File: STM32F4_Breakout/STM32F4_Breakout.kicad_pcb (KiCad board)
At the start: 4 copper layers, 50 x 49.8 mm, 44 parts, among them J1 Conn_01x02, J2 Conn_01x02, J3 Conn_01x02, J4 Conn_02x05_Odd_Even, J5 Conn_01x04, J6 Conn_01x02, U1 AMS1117-3.3, U2 STM32F405RGT6

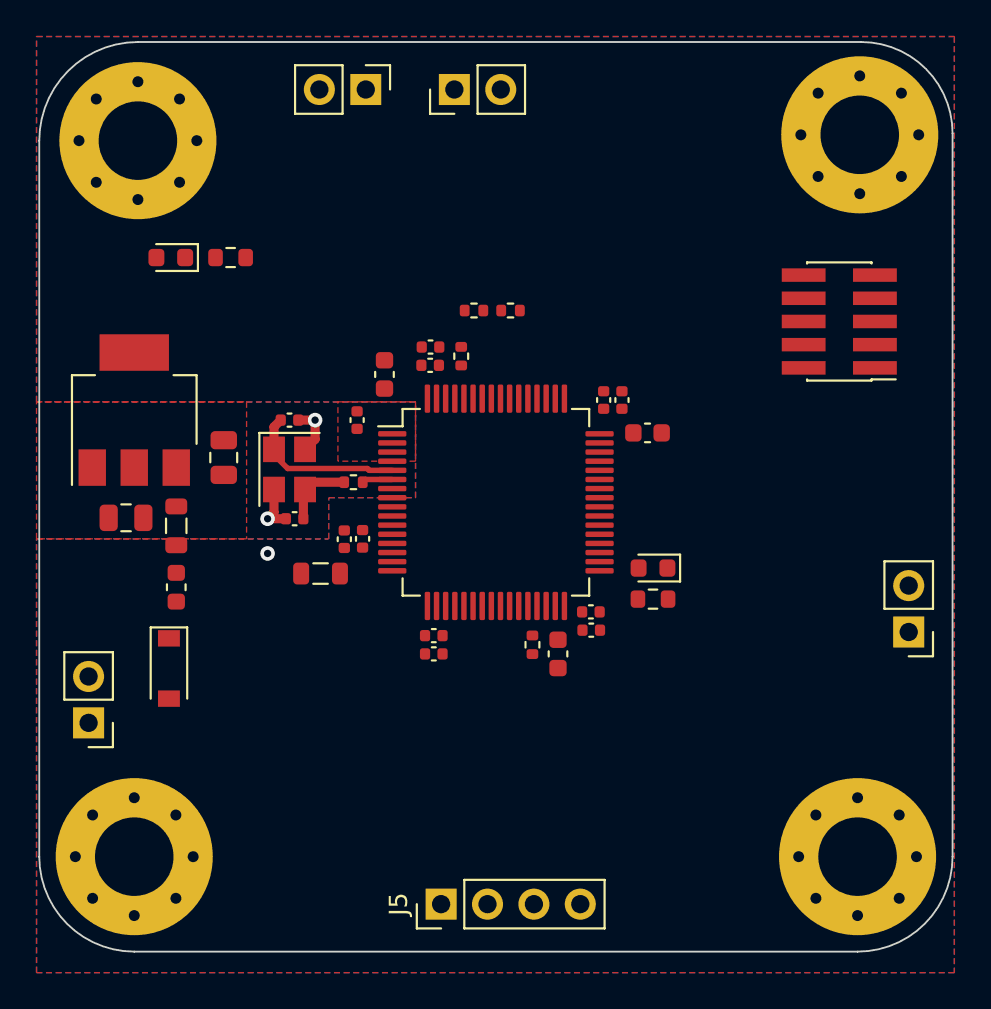
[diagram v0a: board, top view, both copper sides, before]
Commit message: routed power lines and debug connector
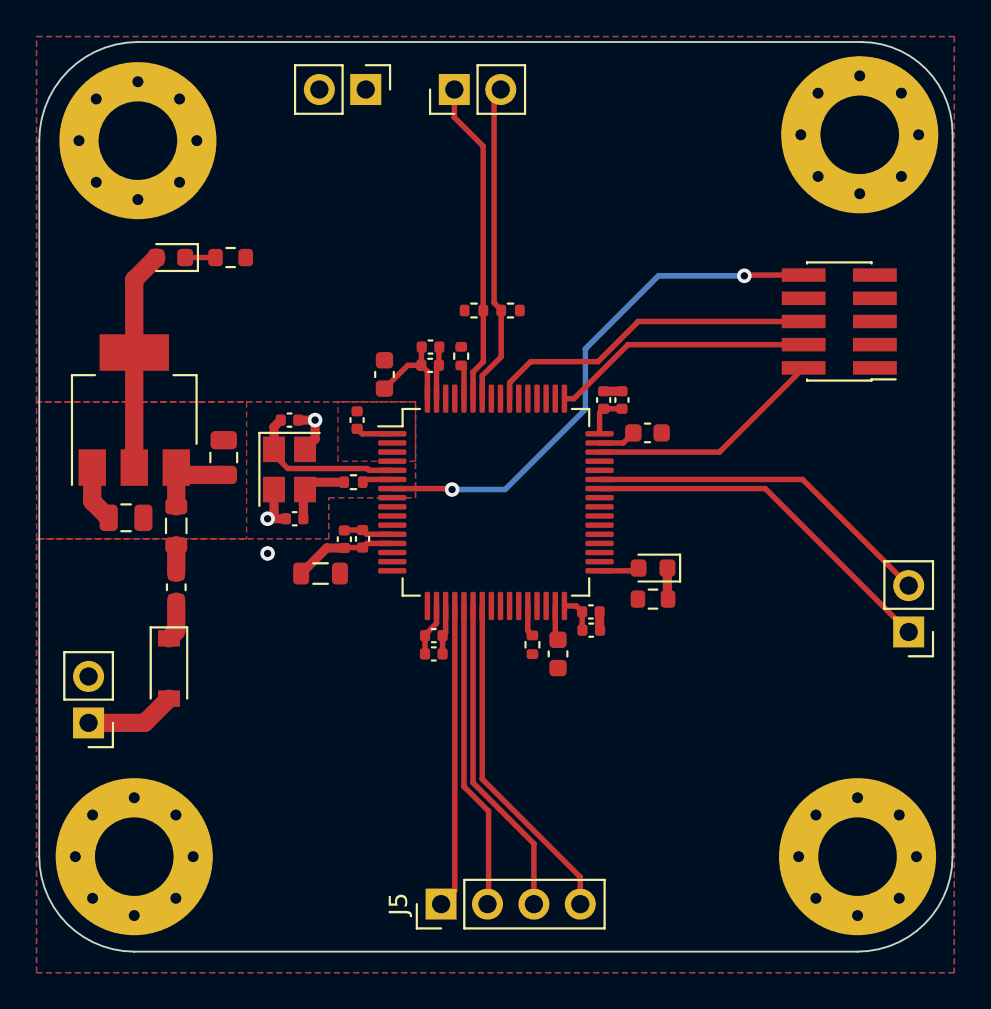
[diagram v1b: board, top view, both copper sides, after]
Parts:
- moved R2 2.00 mm to (86.2, 54.5), turned to 0 degrees
- moved R3 2.00 mm to (84.2, 54.5)
- turned C7 to 0 degrees
- turned C8 to 0 degrees
- turned FB1 to 90 degrees
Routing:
- net NRST: track 0.00 -> 29.3 mm, vias 0 -> 2
- net +3V3: track 0.00 -> 26.8 mm
- net USART1_TX: track 0.00 -> 20.2 mm
- net USART1_RX: track 0.00 -> 19.3 mm
- net SPI1_MOSI: track 0.00 -> 18.5 mm
- net SWO: track 0.00 -> 18.4 mm
- net I2C1_SDA: track 0.00 -> 17.8 mm
- net SPI1_MISO: track 0.00 -> 17.7 mm
- net I2C1_SCL: track 0.00 -> 17.7 mm
- net SPI1_SCK: track 0.00 -> 16.9 mm
- net SPI1_CS: track 0.00 -> 16.6 mm
- net SWCLK: track 0.00 -> 14.3 mm
- net GND: track 7.39 -> 21.0 mm
- net SWDIO: track 0.00 -> 13.1 mm
- net +3.3VA: track 0.00 -> 5.67 mm
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
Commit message: power and ground connections (vias)
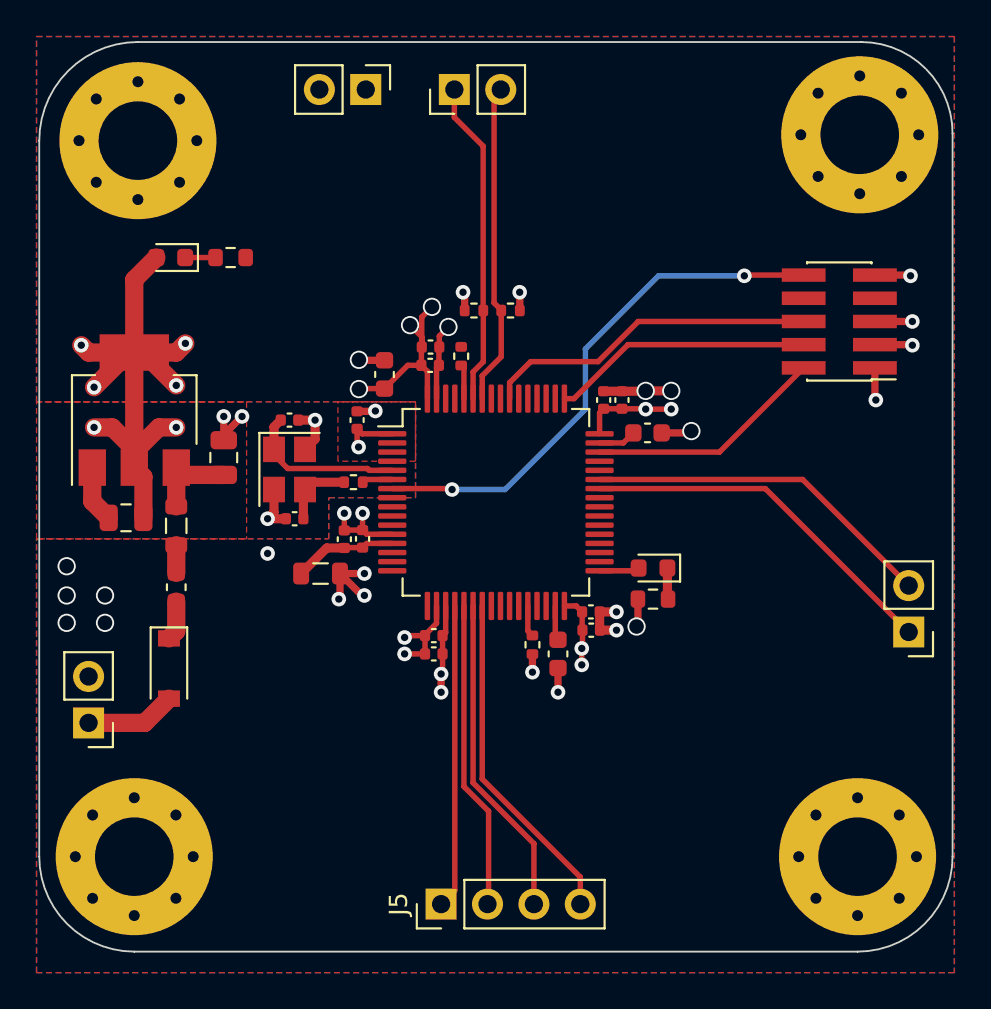
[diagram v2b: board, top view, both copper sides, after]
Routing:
- net +3V3: track 26.8 -> 70.8 mm, vias 0 -> 22
- net GND: track 21.0 -> 48.0 mm, vias 3 -> 28

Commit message: silkscreen labeling; gerber and drill file generation; BoM
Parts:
- moved D1 1.70 mm to (69.2, 74.1)
- moved D2 1.00 mm to (67.6, 52.6)
- moved R1 1.00 mm to (70.9, 52.6)
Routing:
- net VCC: track 4.95 -> 6.65 mm
- net +3V3: track 70.8 -> 69.8 mm
- net Net-(D1-Pad1): track 2.18 -> 3.08 mm
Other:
- board text added: "+"
- board text added: "3V3"
- board text added: "CS"
- board text added: "GND"
- board text added: "I2C"
- board text added: "MISO"
- board text added: "MOSI"
- board text added: "POWER"
- board text added: "RX"
- board text added: "SCK"
- board text added: "SCL"
- board text added: "SDA"
- board text added: "SPI"
- board text added: "STAT"
- board text added: "SWD"
- board text added: "TX"
- board text added: "UART"
- board text added: "VCC"
- board text added: "VIN"
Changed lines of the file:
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@@
       (outputformat 1)
       (mirror false)
-      (drillshape 1)
+      (drillshape 0)
       (scaleselection 1)
-      (outputdirectory "")
+      (outputdirectory "assembly/")
     )
   )
@@
   )
   (footprint "LED_SMD:LED_0603_1608Metric" (layer "F.Cu")
-    (at 67.6 51.6 180)
+    (at 67.6 52.6 180)
     (descr "LED SMD 0603 (1608 Metric), square (rectangular) end terminal, IPC_7351 nominal, (Body size source: http://www.tortai-tech.com/upload/download/2011102023233369053.pdf), generated with kicad-footprint-generator")
     (tags "LED")
@@
   )
   (footprint "Diode_SMD:D_SOD-123" (layer "F.Cu")
-    (at 67.5 74.1 -90)
+    (at 69.2 74.1 -90)
     (descr "SOD-123")
     (tags "SOD-123")
@@
   )
   (footprint "Resistor_SMD:R_0603_1608Metric" (layer "F.Cu")
-    (at 70.875 51.6 180)
+    (at 70.875 52.6 180)
     (descr "Resistor SMD 0603 (1608 Metric), square (rectangular) end terminal, IPC_7351 nominal, (Body size source: IPC-SM-782 page 72, https://www.pcb-3d.com/wordpress/wp-content/uploads/ipc-sm-782a_amendment_1_and_2.pdf), generated with kicad-footprint-generator")
     (tags "resistor")
@@
     )
   )
+  (gr_circle (center 108 57.75) (end 108 57.75) (layer "F.SilkS") (width 0.15) (fill none))
+  (gr_circle (center 78.55 61.225) (end 78.55 61.225) (layer "F.SilkS") (width 0.15) (fill none))
   (gr_line (start 110.4 44.8) (end 110.4 84.4) (layer "Edge.Cuts") (width 0.1))
   (gr_line (start 60.4 84.4) (end 60.4 45.2) (layer "Edge.Cuts") (width 0.1))
@@
   (gr_arc (start 110.4 84.4) (mid 108.876955 88.076955) (end 105.2 89.6) (layer "Edge.Cuts") (width 0.1))
   (gr_arc (start 60.4 45.2) (mid 61.981623 41.381623) (end 65.8 39.8) (layer "Edge.Cuts") (width 0.1))
+  (gr_text "TX" (at 104.6 72.1) (layer "B.SilkS")
+    (effects (font (size 1 1) (thickness 0.15)) (justify mirror))
+  )
+  (gr_text "GND" (at 75.8 45.8 90) (layer "B.SilkS")
+    (effects (font (size 1 1) (thickness 0.15)) (justify mirror))
+  )
+  (gr_text "RX" (at 104.7 69.5) (layer "B.SilkS")
+    (effects (font (size 1 1) (thickness 0.15)) (justify mirror))
+  )
+  (gr_text "MISO" (at 87.5 83.3 90) (layer "B.SilkS")
+    (effects (font (size 1 1) (thickness 0.15)) (justify mirror))
+  )
+  (gr_text "SDA" (at 83.1 45.8 90) (layer "B.SilkS")
+    (effects (font (size 1 1) (thickness 0.15)) (justify mirror))
+  )
+  (gr_text "SCK" (at 84.8 83.5 90) (layer "B.SilkS")
+    (effects (font (size 1 1) (thickness 0.15)) (justify mirror))
+  )
+  (gr_text "VCC" (at 66.5 77.4) (layer "B.SilkS")
+    (effects (font (size 1 1) (thickness 0.15)) (justify mirror))
+  )
+  (gr_text "CS" (at 82.3 83.4 90) (layer "B.SilkS")
+    (effects (font (size 1 1) (thickness 0.15)) (justify mirror))
+  )
+  (gr_text "MOSI" (at 90 83.3 90) (layer "B.SilkS")
+    (effects (font (size 1 1) (thickness 0.15)) (justify mirror))
+  )
+  (gr_text "GND" (at 66.6 74.5) (layer "B.SilkS")
+    (effects (font (size 1 1) (thickness 0.15)) (justify mirror))
+  )
+  (gr_text "SCL" (at 86.2 45.9 90) (layer "B.SilkS")
+    (effects (font (size 1 1) (thickness 0.15)) (justify mirror))
+  )
+  (gr_text "3V3" (at 78.6 45.8 90) (layer "B.SilkS")
+    (effects (font (size 1 1) (thickness 0.15)) (justify mirror))
+  )
+  (gr_text "+" (at 66.2 53.4) (layer "F.SilkS")
+    (effects (font (size 1 1) (thickness 0.15)))
+  )
+  (gr_text "UART" (at 105.1 70.8 90) (layer "F.SilkS")
+    (effects (font (size 1 1) (thickness 0.15)))
+  )
+  (gr_text "I2C" (at 84.7 45) (layer "F.SilkS")
+    (effects (font (size 1 1) (thickness 0.15)))
+  )
+  (gr_text "STAT" (at 93.9 67.1) (layer "F.SilkS")
+    (effects (font (size 1 1) (thickness 0.15)))
+  )
+  (gr_text "+" (at 92.5 69.2) (layer "F.SilkS")
+    (effects (font (size 1 1) (thickness 0.15)))
+  )
+  (gr_text "VIN" (at 65.8 75.3 90) (layer "F.SilkS")
+    (effects (font (size 1 1) (thickness 0.15)))
+  )
+  (gr_text "3V3" (at 67.4 51.1) (layer "F.SilkS")
+    (effects (font (size 1 1) (thickness 0.15)))
+  )
+  (gr_text "+" (at 70.4 76.4) (layer "F.SilkS")
+    (effects (font (size 1 1) (thickness 0.15)))
+  )
+  (gr_text "SPI" (at 86 84.4) (layer "F.SilkS")
+    (effects (font (size 1 1) (thickness 0.15)))
+  )
+  (gr_text "POWER" (at 77 45.1) (layer "F.SilkS")
+    (effects (font (size 1 1) (thickness 0.15)))
+  )
+  (gr_text "SWD" (at 104.2 60) (layer "F.SilkS")
+    (effects (font (size 1 1) (thickness 0.15)))
+  )
   (segment (start 70.5 61.3) (end 71.5 60.3) (width 0.4) (layer "F.Cu") (net 1))
   (segment (start 91.3 58.92) (end 92.3 58.92) (width 0.5) (layer "F.Cu") (net 1))
@@
   (segment (start 94.7875 70.2625) (end 94.825 70.3) (width 0.5) (layer "F.Cu") (net 2))
   (segment (start 94.7875 68.6) (end 94.7875 70.2625) (width 0.5) (layer "F.Cu") (net 2))
-  (segment (start 68.3875 51.6) (end 70.05 51.6) (width 0.3) (layer "F.Cu") (net 3))
+  (segment (start 68.3875 52.6) (end 70.05 52.6) (width 0.3) (layer "F.Cu") (net 3))
   (segment (start 83.65 57.66) (end 83.5 57.51) (width 0.3) (layer "F.Cu") (net 4))
   (segment (start 83.65 59.325) (end 83.65 57.66) (width 0.3) (layer "F.Cu") (net 4))
@@
   (segment (start 84.15 57.865894) (end 84.71 57.305894) (width 0.3) (layer "F.Cu") (net 8))
   (segment (start 93.58 59.88) (end 93.6 59.9) (width 0.3) (layer "F.Cu") (net 9))
-  (segment (start 65.6 52.8125) (end 66.8125 51.6) (width 1) (layer "F.Cu") (net 9))
+  (segment (start 65.6 53.8125) (end 66.8125 52.6) (width 1) (layer "F.Cu") (net 9))
   (segment (start 86.71 53.51) (end 86.7 53.5) (width 0.4) (layer "F.Cu") (net 9))
   (segment (start 66.1 56.8) (end 67.9 58.6) (width 1) (layer "F.Cu") (net 9))
@@
   (segment (start 65.6 63.1) (end 65.6 62.1) (width 1) (layer "F.Cu") (net 9))
   (segment (start 90.14 72) (end 90.14 72.96) (width 0.3) (layer "F.Cu") (net 9))
-  (segment (start 65.6 56.8) (end 65.6 52.8125) (width 1) (layer "F.Cu") (net 9))
   (segment (start 82.65 72.13) (end 82.48 72.3) (width 0.3) (layer "F.Cu") (net 9))
   (segment (start 65.6 62.1) (end 64.4 60.9) (width 1) (layer "F.Cu") (net 9))
@@
   (segment (start 80.575 57.5) (end 79.3 58.775) (width 0.3) (layer "F.Cu") (net 9))
   (segment (start 79.725 61.25) (end 78.07 61.25) (width 0.3) (layer "F.Cu") (net 9))
+  (segment (start 65.6 56.8) (end 65.6 53.8) (width 1) (layer "F.Cu") (net 9))
   (segment (start 90.14 72.96) (end 90.1 73) (width 0.3) (layer "F.Cu") (net 9))
   (segment (start 65.6 63.1) (end 65.6 56.8) (width 1) (layer "F.Cu") (net 9))
@@
   (segment (start 87.298959 57.3) (end 90.992894 57.3) (width 0.3) (layer "F.Cu") (net 58))
   (segment (start 67.9 67.35) (end 67.9 68.8625) (width 1) (layer "F.Cu") (net 63))
-  (segment (start 67.9 72.05) (end 67.5 72.45) (width 1) (layer "F.Cu") (net 64))
+  (segment (start 67.9 72.05) (end 68.8 72.05) (width 1) (layer "F.Cu") (net 64))
   (segment (start 67.9 70.4375) (end 67.9 72.05) (width 1) (layer "F.Cu") (net 64))
-  (segment (start 66.175 77.075) (end 67.5 75.75) (width 1) (layer "F.Cu") (net 65))
-  (segment (start 63.1 77.075) (end 66.175 77.075) (width 1) (layer "F.Cu") (net 65))
+  (segment (start 68.8 72.05) (end 69.2 72.45) (width 1) (layer "F.Cu") (net 64))
+  (segment (start 67.875 77.075) (end 69.2 75.75) (width 1) (layer "F.Cu") (net 65))
+  (segment (start 63.1 77.075) (end 67.875 77.075) (width 1) (layer "F.Cu") (net 65))
   (zone (net 1) (net_name "GND") (layer "F.Cu") (hatch edge 0.508)
     (connect_pads (clearance 0.508))
